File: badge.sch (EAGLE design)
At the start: 3 parts

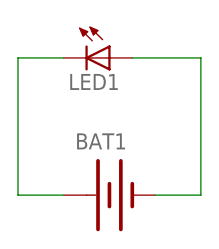
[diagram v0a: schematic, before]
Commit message: Fixed polarity
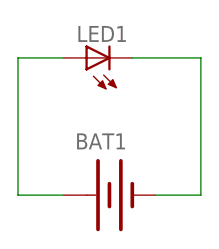
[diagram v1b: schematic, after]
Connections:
- net GND: now also LED1.C; no longer LED1.A
- net N$2: now also LED1.A; no longer LED1.C
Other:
- moved on the sheet: LED1
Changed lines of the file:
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@@
 <instances>
 <instance part="BAT1" gate="G$1" x="20.32" y="15.24"/>
-<instance part="LED1" gate="G$1" x="20.32" y="30.48" rot="R270"/>
+<instance part="LED1" gate="G$1" x="17.78" y="30.48" rot="R90"/>
 <instance part="U$1" gate="G$1" x="35.56" y="43.18"/>
 </instances>
@@
 <wire x1="25.4" y1="15.24" x2="30.48" y2="15.24" width="0.1524" layer="91"/>
 <wire x1="30.48" y1="15.24" x2="30.48" y2="30.48" width="0.1524" layer="91"/>
-<pinref part="LED1" gate="G$1" pin="A"/>
-<wire x1="30.48" y1="30.48" x2="22.86" y2="30.48" width="0.1524" layer="91"/>
+<pinref part="LED1" gate="G$1" pin="C"/>
+<wire x1="22.86" y1="30.48" x2="30.48" y2="30.48" width="0.1524" layer="91"/>
 </segment>
 </net>
 <net name="N$2" class="0">
 <segment>
-<pinref part="LED1" gate="G$1" pin="C"/>
-<wire x1="15.24" y1="30.48" x2="10.16" y2="30.48" width="0.1524" layer="91"/>
 <wire x1="10.16" y1="30.48" x2="10.16" y2="15.24" width="0.1524" layer="91"/>
 <pinref part="BAT1" gate="G$1" pin="+"/>
 <wire x1="10.16" y1="15.24" x2="15.24" y2="15.24" width="0.1524" layer="91"/>
+<pinref part="LED1" gate="G$1" pin="A"/>
+<wire x1="10.16" y1="30.48" x2="15.24" y2="30.48" width="0.1524" layer="91"/>
 </segment>
 </net>
